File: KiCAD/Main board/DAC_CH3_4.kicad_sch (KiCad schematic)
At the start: 43 parts, among them U1 PCM1789, U3 OPA1632DR, U4 OPA1632DR

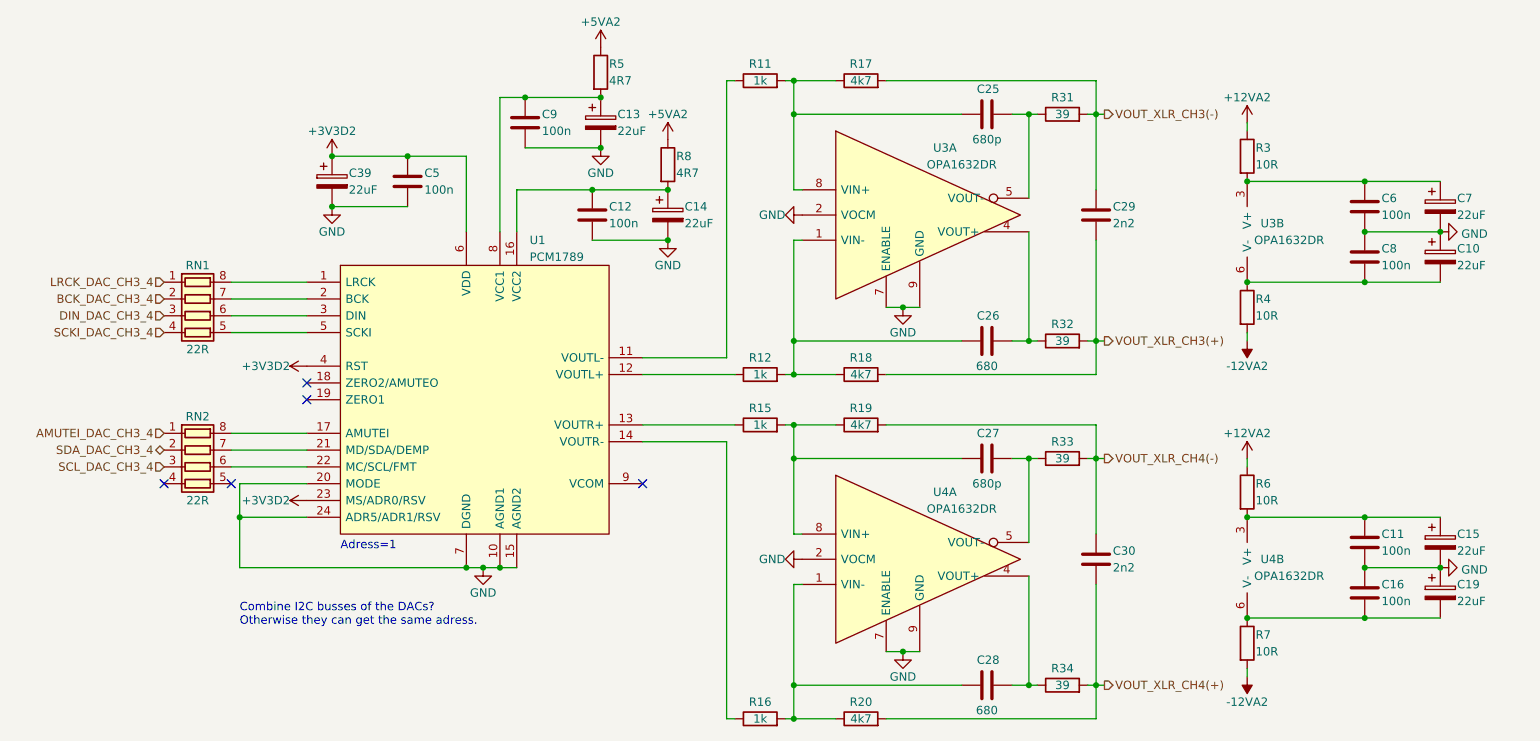
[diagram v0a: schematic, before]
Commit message: Finalizer main board schematic exept passive order links. Schematic ready for review
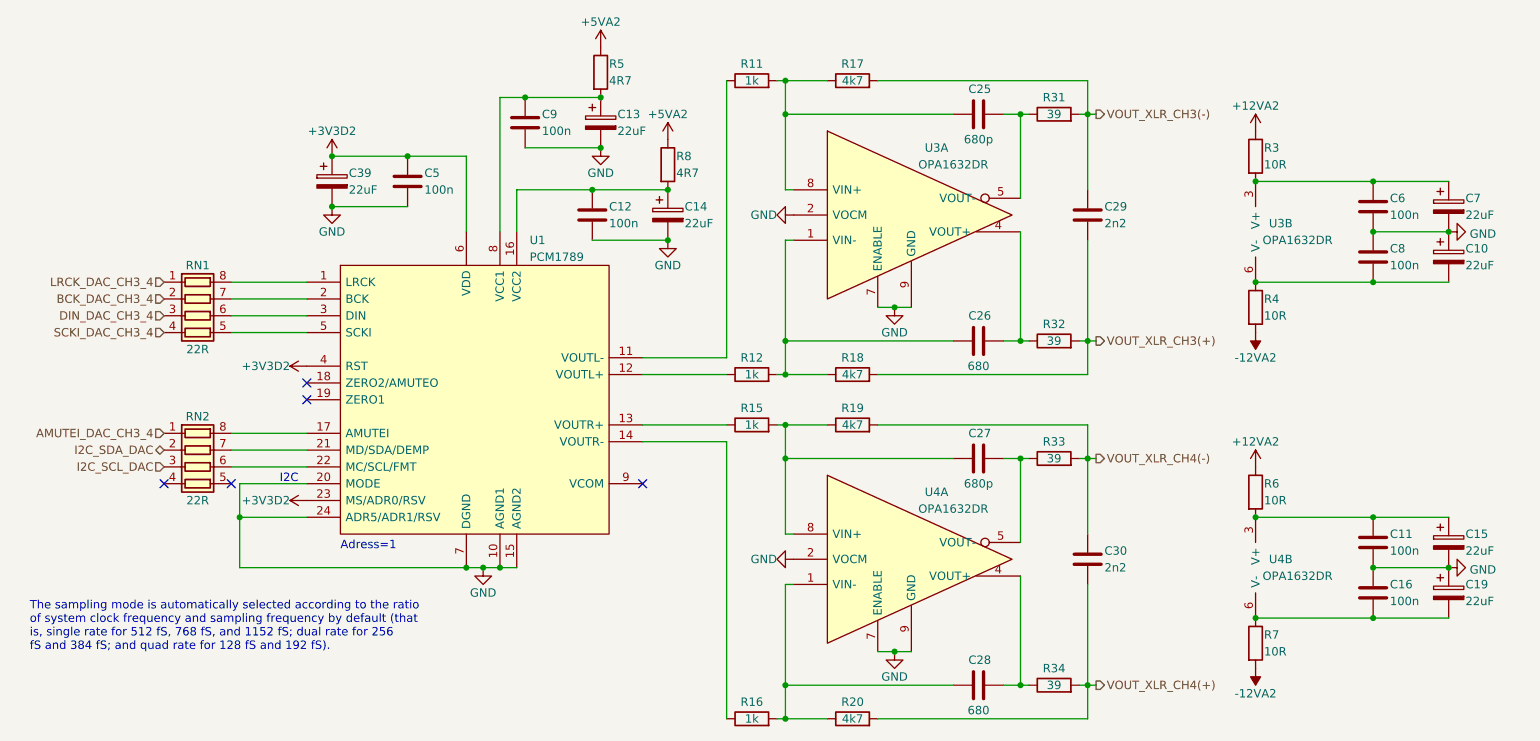
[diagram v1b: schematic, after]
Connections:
- net SCL_DAC_CH3_4 renamed I2C_SCL_DAC
- net SDA_DAC_CH3_4 renamed I2C_SDA_DAC
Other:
- note added: "I2C"
- note added: "The sampling mode is automatically selected according to the ratio of system clock frequency and sampling frequency by default (that is, single rate for 512 fS, 768 fS, and 1152 fS; dual rate for 256 fS and 384 fS; and quad rate for 128 fS and 192 fS)."
- note removed: "Combine I2C busses of the DACs? Otherwise they can get the same adress."
- moved on the sheet: C10, C11, C15, C16, C19, C25, C26, C27, C28, C29, C30, C6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

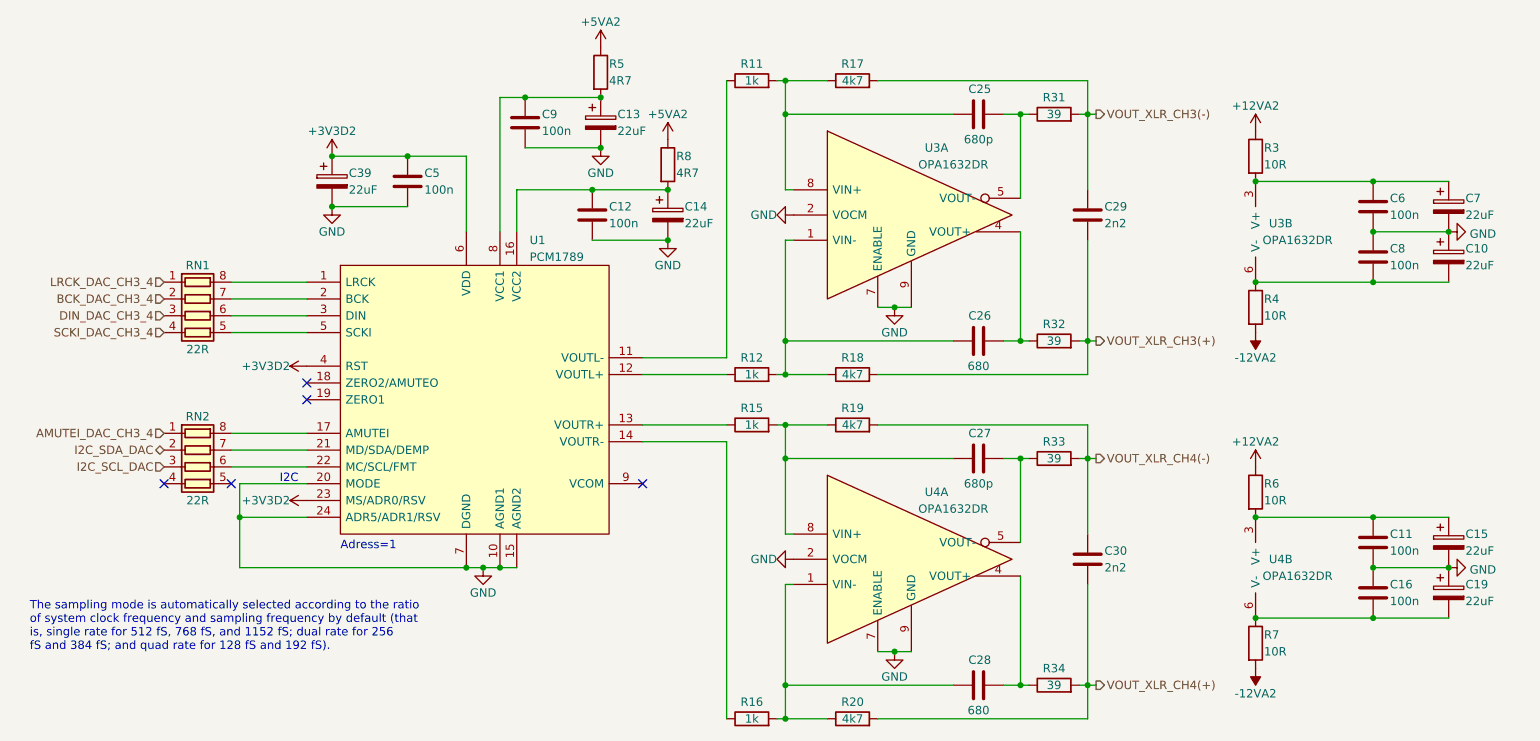
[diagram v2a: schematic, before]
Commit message: Added component links
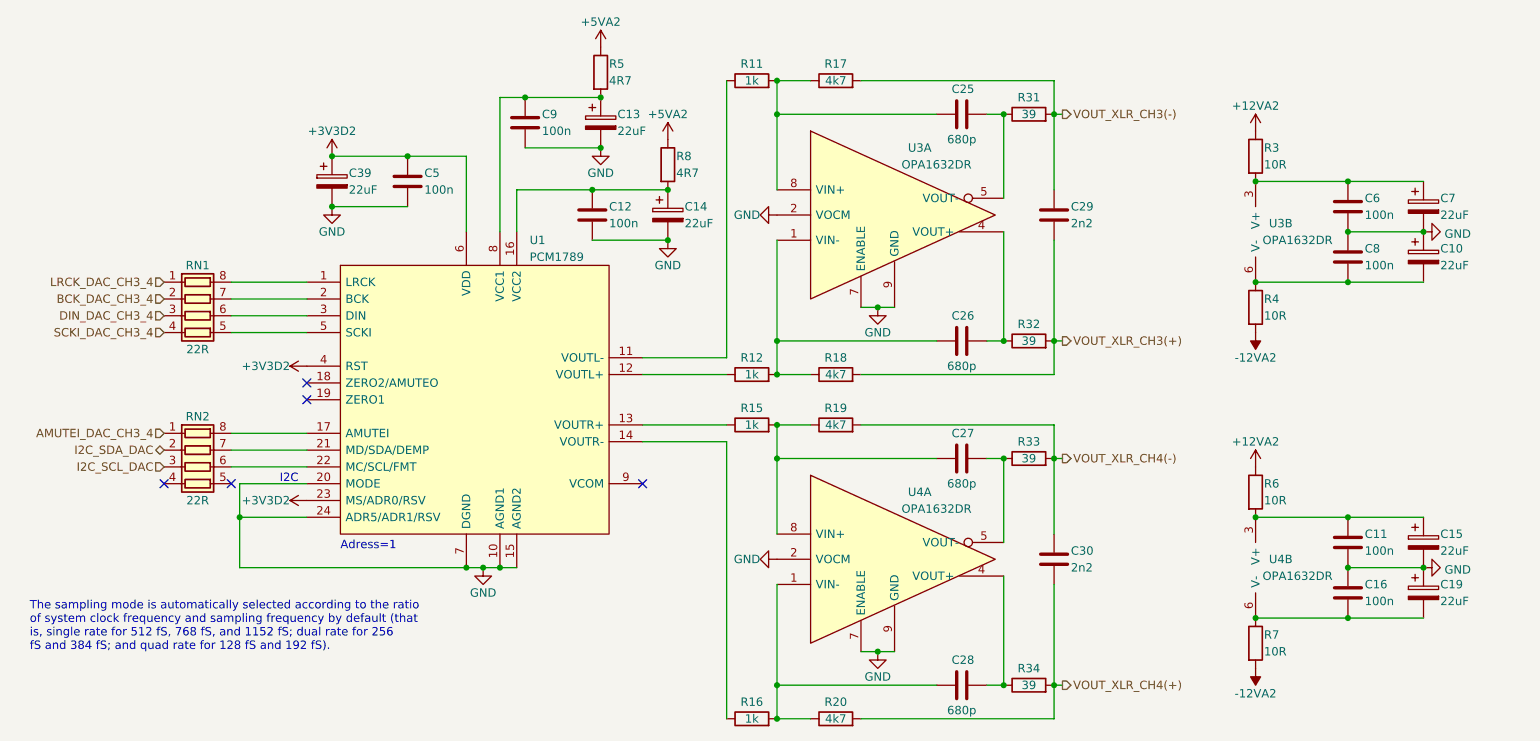
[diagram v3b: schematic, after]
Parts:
- C26, C28: value 680 -> 680p
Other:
- moved on the sheet: C10, C11, C15, C16, C19, C25, C26, C27, C28, C29, C30, C6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

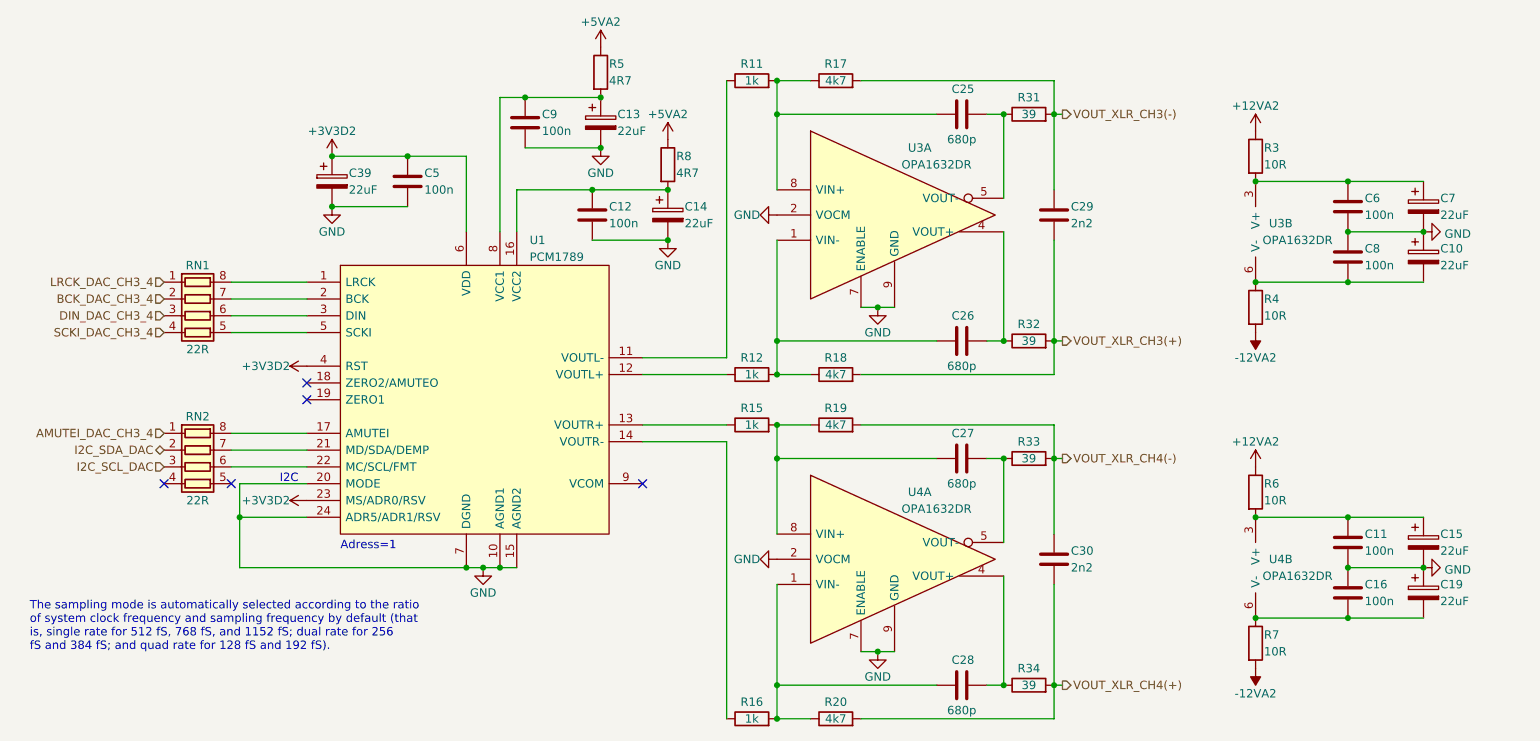
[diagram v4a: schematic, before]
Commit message: Added rotary encoder and pull-up
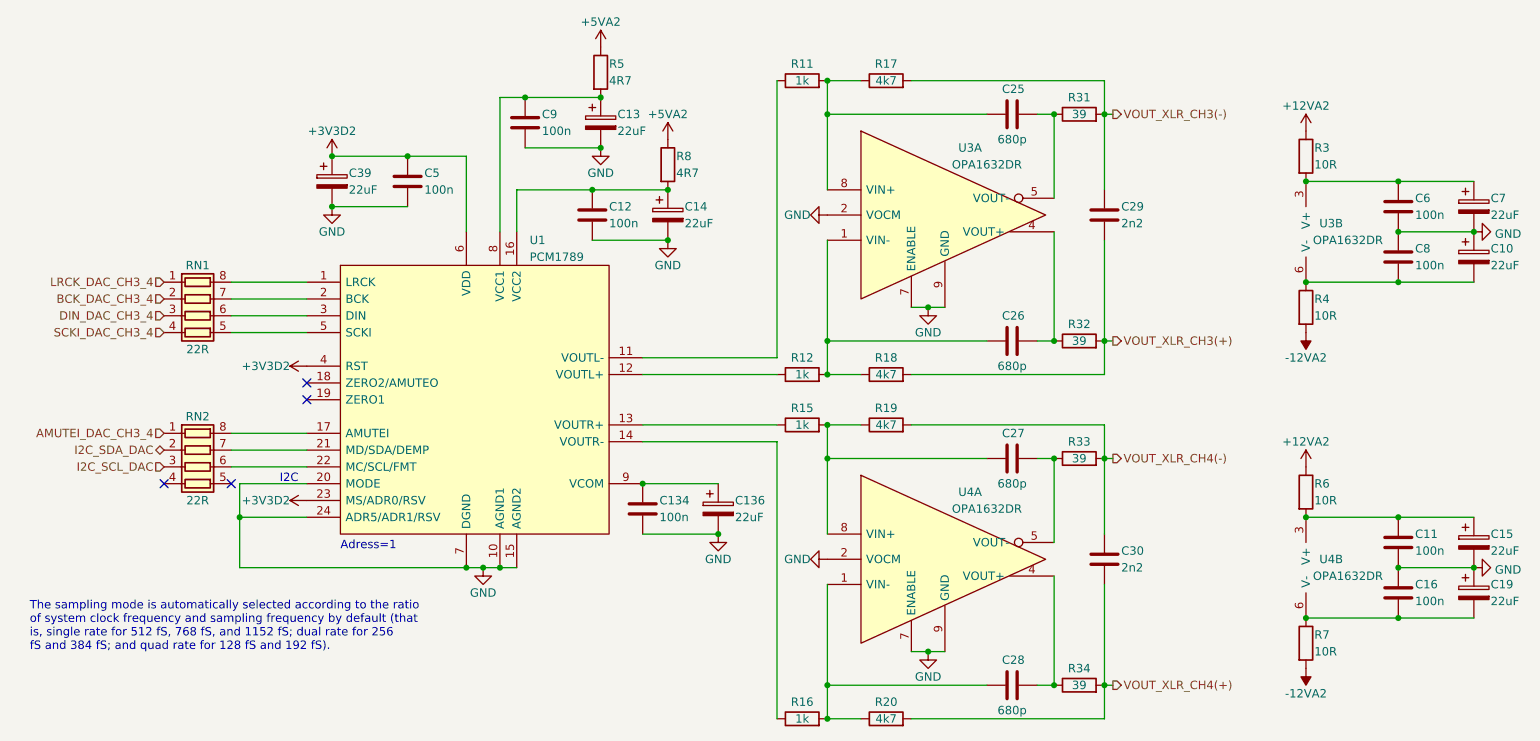
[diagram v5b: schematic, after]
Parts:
- added C134: 100n, Capacitor_SMD:C_0402_1005Metric, symbol Device:C
- added C136: 22uF, Capacitor_THT:CP_Radial_D5.0mm_P2.00mm, symbol Device:C_Polarized
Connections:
- net GND: now also C134.2, C136.2
- net at U1.9 (VCOM): now also C134.1, C136.1
- no-connect marks 5 -> 4
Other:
- moved on the sheet: C10, C11, C15, C16, C19, C25, C26, C27, C28, C29, C30, C6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

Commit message: PCB finished + gerber
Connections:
- net AMUTEI_DAC_CH3_4: now also RN2.3 (R3.1); no longer RN2.1 (R1.1)
- net I2C_SCL_DAC: now also RN2.2 (R2.1); no longer RN2.3 (R3.1)
- net I2C_SDA_DAC: now also RN2.1 (R1.1); no longer RN2.2 (R2.1)
- net at RN2.6 (R3.2): now also U1.17 (AMUTEI); no longer U1.22 (MC/SCL/FMT)
- net at RN2.7 (R2.2): now also U1.22 (MC/SCL/FMT); no longer U1.21 (MD/SDA/DEMP)
- net at RN2.8 (R1.2): now also U1.21 (MD/SDA/DEMP); no longer U1.17 (AMUTEI)
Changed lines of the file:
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@@
+    (stroke (width 0) (type default))
+  )
+  (wire (pts (xy 46.355 83.82) (xy 54.61 83.82))
+    (stroke (width 0) (type default))
+  )
+  (wire (pts (xy 43.18 80.01) (xy 46.355 80.01))
     (stroke (width 0) (type default))
   )
@@
     (stroke (width 0) (type default))
   )
+  (wire (pts (xy 47.625 80.01) (xy 54.61 80.01))
+    (stroke (width 0) (type default))
+  )
   (wire (pts (xy 133.35 29.21) (xy 133.35 40.64))
     (stroke (width 0) (type default))
   )
+  (wire (pts (xy 43.18 82.55) (xy 49.53 82.55))
+    (stroke (width 0) (type default))
+  )
   (wire (pts (xy 175.26 68.58) (xy 175.26 63.5))
     (stroke (width 0) (type default))
@@
     (stroke (width 0) (type default))
   )
-  (wire (pts (xy 43.18 80.01) (xy 54.61 80.01))
-    (stroke (width 0) (type default))
-  )
   (wire (pts (xy 105.41 68.58) (xy 125.73 68.58))
     (stroke (width 0) (type default))
@@
     (stroke (width 0) (type default))
   )
+  (wire (pts (xy 43.18 77.47) (xy 47.625 77.47))
+    (stroke (width 0) (type default))
+  )
   (wire (pts (xy 205.74 54.61) (xy 219.71 54.61))
     (stroke (width 0) (type default))
@@
     (stroke (width 0) (type default))
   )
-  (wire (pts (xy 43.18 77.47) (xy 54.61 77.47))
+  (wire (pts (xy 49.53 82.55) (xy 49.53 77.47))
     (stroke (width 0) (type default))
   )
@@
     (stroke (width 0) (type default))
   )
-  (wire (pts (xy 43.18 82.55) (xy 54.61 82.55))
-    (stroke (width 0) (type default))
-  )
   (wire (pts (xy 133.35 63.5) (xy 133.35 68.58))
     (stroke (width 0) (type default))
@@
     (stroke (width 0) (type default))
   )
+  (wire (pts (xy 54.61 82.55) (xy 54.61 83.82))
+    (stroke (width 0) (type default))
+  )
   (wire (pts (xy 219.71 105.41) (xy 231.14 105.41))
     (stroke (width 0) (type default))
@@
     (stroke (width 0) (type default))
   )
+  (wire (pts (xy 47.625 77.47) (xy 47.625 80.01))
+    (stroke (width 0) (type default))
+  )
+  (wire (pts (xy 49.53 77.47) (xy 54.61 77.47))
+    (stroke (width 0) (type default))
+  )
   (wire (pts (xy 125.73 24.13) (xy 125.73 66.04))
     (stroke (width 0) (type default))
@@
   )
   (wire (pts (xy 165.1 81.28) (xy 167.64 81.28))
+    (stroke (width 0) (type default))
+  )
+  (wire (pts (xy 46.355 80.01) (xy 46.355 83.82))
     (stroke (width 0) (type default))
   )
@@
     (effects (font (size 1.27 1.27)) (justify left))
   )
-  (hierarchical_label "I2C_SDA_DAC" (shape bidirectional) (at 33.02 80.01 180) (fields_autoplaced)
-    (effects (font (size 1.27 1.27)) (justify right))
-  )
-  (hierarchical_label "I2C_SCL_DAC" (shape input) (at 33.02 82.55 180) (fields_autoplaced)
+  (hierarchical_label "I2C_SDA_DAC" (shape bidirectional) (at 33.02 77.47 180) (fields_autoplaced)
+    (effects (font (size 1.27 1.27)) (justify right))
+  )
+  (hierarchical_label "I2C_SCL_DAC" (shape input) (at 33.02 80.01 180) (fields_autoplaced)
     (effects (font (size 1.27 1.27)) (justify right))
   )
@@
     (effects (font (size 1.27 1.27)) (justify right))
   )
-  (hierarchical_label "AMUTEI_DAC_CH3_4" (shape input) (at 33.02 77.47 180) (fields_autoplaced)
-    (effects (font (size 1.27 1.27)) (justify right))
-  )
+  (hierarchical_label "AMUTEI_DAC_CH3_4" (shape input) (at 33.02 82.55 180) (fields_autoplaced)
+    (effects (font (size 1.27 1.27)) (justify right))
+  )
